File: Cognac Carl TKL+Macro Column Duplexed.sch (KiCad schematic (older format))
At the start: 277 parts

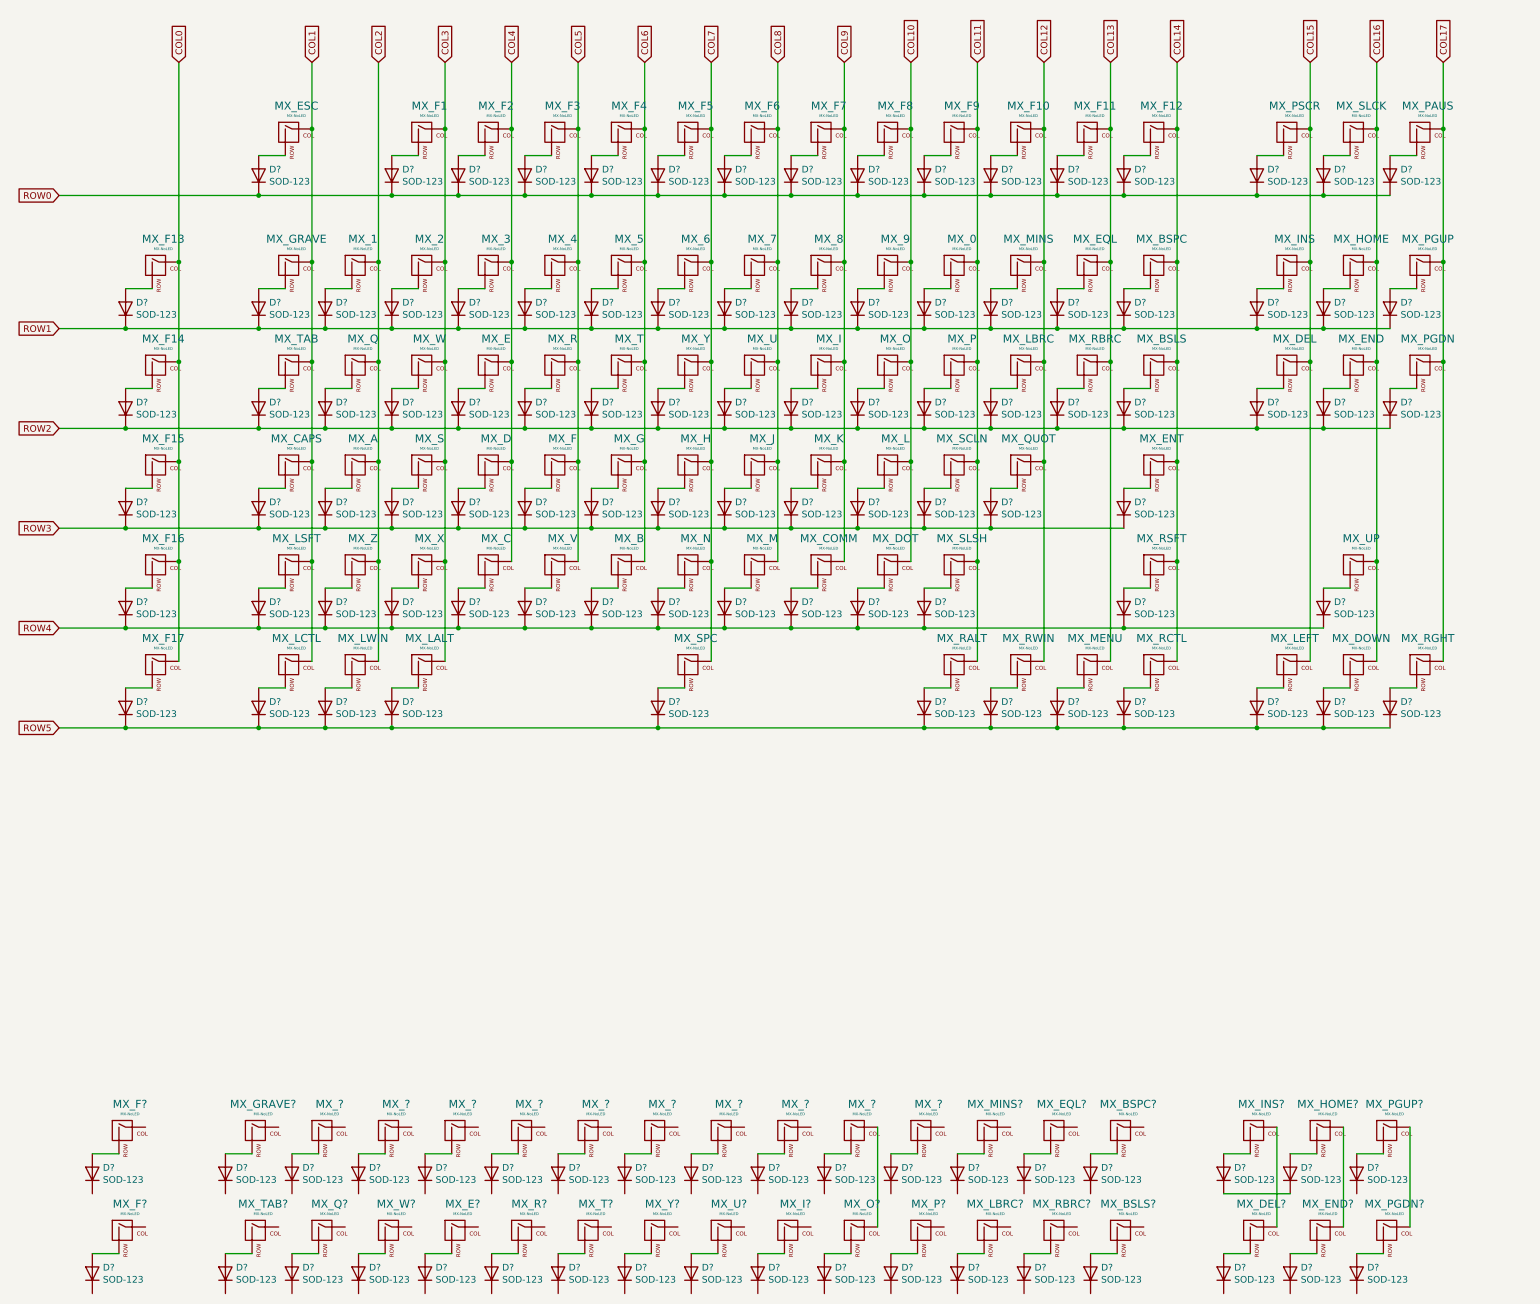
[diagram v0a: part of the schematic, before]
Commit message: Added Type-C connector, footprints
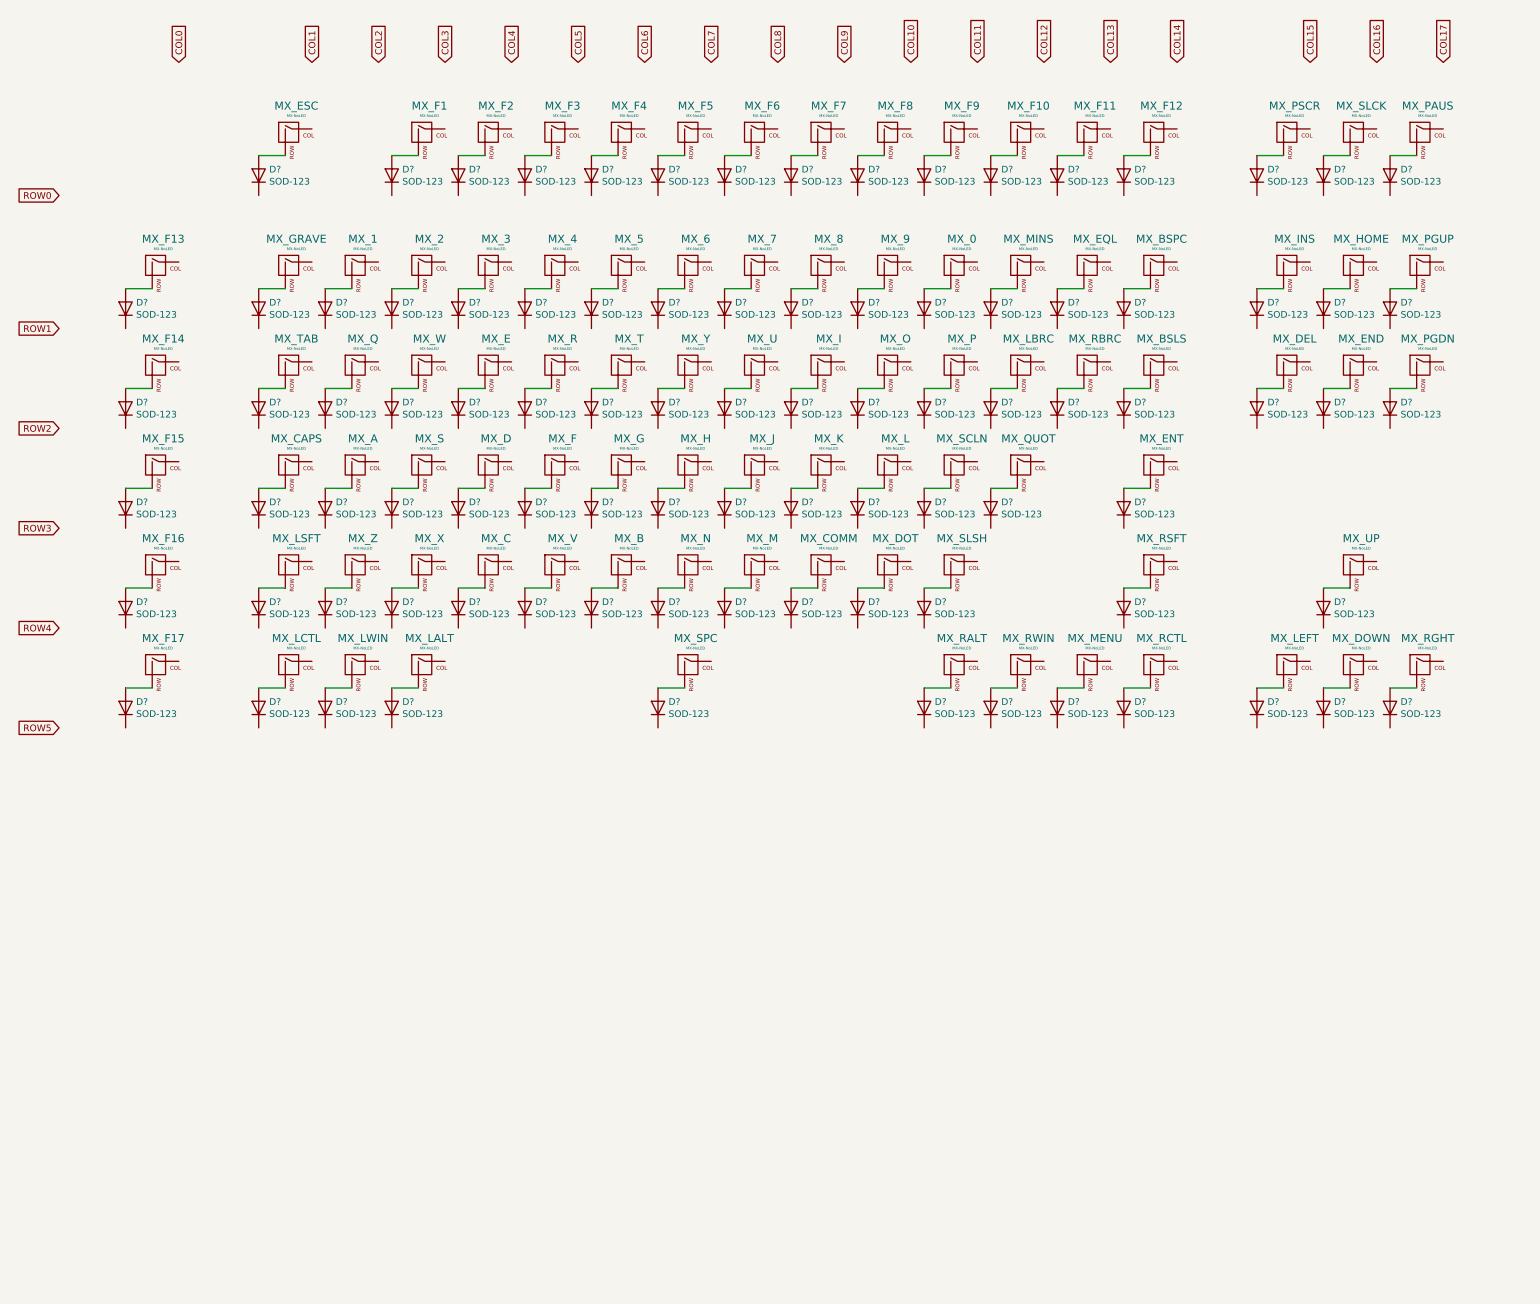
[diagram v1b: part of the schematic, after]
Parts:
- removed D? (x36): SOD-123, symbol Device:D
- removed MX_? (x10), MX_BSLS?, MX_BSPC?, MX_DEL?, MX_E?, MX_END?, MX_EQL?, MX_F? (x2), MX_GRAVE?, MX_HOME?, MX_I?, MX_INS?, MX_LBRC?, MX_MINS?, MX_O?, MX_P?, MX_PGDN?, MX_PGUP?, MX_Q?, MX_R?, MX_RBRC?, MX_T?, MX_TAB?, MX_U?, MX_W?, MX_Y?: MX-NoLED, symbol MX_Alps_Hybrid:MX-NoLED
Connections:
- net COL0: no longer MX_F13.1 (COL), MX_F14.1 (COL), MX_F15.1 (COL), MX_F16.1 (COL), MX_F17.1 (COL)
- net COL1: no longer MX_CAPS.1 (COL), MX_ESC.1 (COL), MX_GRAVE.1 (COL), MX_LCTL.1 (COL), MX_LSFT.1 (COL), MX_TAB.1 (COL)
- net COL10: no longer MX_9.1 (COL), MX_DOT.1 (COL), MX_F8.1 (COL), MX_L.1 (COL), MX_O.1 (COL)
- net COL11: no longer MX_0.1 (COL), MX_F9.1 (COL), MX_P.1 (COL), MX_RALT.1 (COL), MX_SCLN.1 (COL), MX_SLSH.1 (COL)
- net COL12: no longer MX_F10.1 (COL), MX_LBRC.1 (COL), MX_MINS.1 (COL), MX_QUOT.1 (COL), MX_RWIN.1 (COL)
- net COL13: no longer MX_EQL.1 (COL), MX_F11.1 (COL), MX_MENU.1 (COL), MX_RBRC.1 (COL)
- net COL14: no longer MX_BSLS.1 (COL), MX_BSPC.1 (COL), MX_ENT.1 (COL), MX_F12.1 (COL), MX_RCTL.1 (COL), MX_RSFT.1 (COL)
- net COL15: no longer MX_DEL.1 (COL), MX_INS.1 (COL), MX_LEFT.1 (COL), MX_PSCR.1 (COL)
- net COL16: no longer MX_DOWN.1 (COL), MX_END.1 (COL), MX_HOME.1 (COL), MX_SLCK.1 (COL), MX_UP.1 (COL)
- net COL17: no longer MX_PAUS.1 (COL), MX_PGDN.1 (COL), MX_PGUP.1 (COL), MX_RGHT.1 (COL)
- net COL2: no longer MX_1.1 (COL), MX_A.1 (COL), MX_LWIN.1 (COL), MX_Q.1 (COL), MX_Z.1 (COL)
- net COL3: no longer MX_2.1 (COL), MX_F1.1 (COL), MX_LALT.1 (COL), MX_S.1 (COL), MX_W.1 (COL), MX_X.1 (COL)
- net COL4: no longer MX_3.1 (COL), MX_C.1 (COL), MX_D.1 (COL), MX_E.1 (COL), MX_F2.1 (COL)
- net COL5: no longer MX_4.1 (COL), MX_F.1 (COL), MX_F3.1 (COL), MX_R.1 (COL), MX_V.1 (COL)
- net COL6: no longer MX_5.1 (COL), MX_B.1 (COL), MX_F4.1 (COL), MX_G.1 (COL), MX_T.1 (COL)
- net COL7: no longer MX_6.1 (COL), MX_F5.1 (COL), MX_H.1 (COL), MX_N.1 (COL), MX_SPC.1 (COL), MX_Y.1 (COL)
- net COL8: no longer MX_7.1 (COL), MX_F6.1 (COL), MX_J.1 (COL), MX_M.1 (COL), MX_U.1 (COL)
- net COL9: no longer MX_8.1 (COL), MX_COMM.1 (COL), MX_F7.1 (COL), MX_I.1 (COL), MX_K.1 (COL)
- net ROW0: no longer D?.1 (K), D?.1 (K), D?.1 (K), D?.1 (K), D?.1 (K), D?.1 (K), D?.1 (K), D?.1 (K), D?.1 (K), D?.1 (K), D?.1 (K), D?.1 (K), D?.1 (K), D?.1 (K), D?.1 (K), D?.1 (K)
- net ROW1: no longer D?.1 (K), D?.1 (K), D?.1 (K), D?.1 (K), D?.1 (K), D?.1 (K), D?.1 (K), D?.1 (K), D?.1 (K), D?.1 (K), D?.1 (K), D?.1 (K), D?.1 (K), D?.1 (K), D?.1 (K), D?.1 (K), D?.1 (K), D?.1 (K)
- net ROW2: no longer D?.1 (K), D?.1 (K), D?.1 (K), D?.1 (K), D?.1 (K), D?.1 (K), D?.1 (K), D?.1 (K), D?.1 (K), D?.1 (K), D?.1 (K), D?.1 (K), D?.1 (K), D?.1 (K), D?.1 (K), D?.1 (K), D?.1 (K), D?.1 (K)
- net ROW3: no longer D?.1 (K), D?.1 (K), D?.1 (K), D?.1 (K), D?.1 (K), D?.1 (K), D?.1 (K), D?.1 (K), D?.1 (K), D?.1 (K), D?.1 (K), D?.1 (K), D?.1 (K), D?.1 (K)
- net ROW4: no longer D?.1 (K), D?.1 (K), D?.1 (K), D?.1 (K), D?.1 (K), D?.1 (K), D?.1 (K), D?.1 (K), D?.1 (K), D?.1 (K), D?.1 (K), D?.1 (K), D?.1 (K), D?.1 (K)
- net ROW5: no longer D?.1 (K), D?.1 (K), D?.1 (K), D?.1 (K), D?.1 (K), D?.1 (K), D?.1 (K), D?.1 (K), D?.1 (K), D?.1 (K), D?.1 (K), D?.1 (K)
